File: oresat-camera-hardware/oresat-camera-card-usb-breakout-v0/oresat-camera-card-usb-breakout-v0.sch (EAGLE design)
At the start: 4 parts, among them J2 USB_A_SMT_FEMALE, J3 2-1734592-0

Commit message: first draft finished
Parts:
- added TP1: TEST-POINTPOGO_PTH, SparkFun-Connectors:TEST-POINTPOGO_PTH
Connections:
- new net N$2: J3.17, TP1.1
- net GND: no longer J3.17
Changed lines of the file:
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@@
 <part name="C1" library="oresat-rcl" deviceset="C-EU" device="0603-A" value="100nf"/>
 <part name="GND6" library="SparkFun-PowerSymbols" deviceset="GND" device=""/>
+<part name="TP1" library="SparkFun-Connectors" deviceset="TEST-POINT" device="POGO_PTH"/>
 </parts>
 <sheets>
@@
 <instance part="GND6" gate="1" x="86.36" y="-15.24" smashed="yes">
 <attribute name="VALUE" x="86.36" y="-15.494" size="1.778" layer="96" align="top-center"/>
+</instance>
+<instance part="TP1" gate="G$1" x="55.88" y="27.94" smashed="yes">
+<attribute name="NAME" x="53.34" y="30.48" size="1.778" layer="95" font="vector"/>
 </instance>
 </instances>
@@
 </segment>
 <segment>
-<pinref part="J3" gate="G$1" pin="17"/>
-<wire x1="45.72" y1="27.94" x2="48.26" y2="27.94" width="0.1524" layer="91"/>
-<wire x1="48.26" y1="27.94" x2="48.26" y2="30.48" width="0.1524" layer="91"/>
 <pinref part="J3" gate="G$1" pin="PAD"/>
 <wire x1="48.26" y1="30.48" x2="48.26" y2="33.02" width="0.1524" layer="91"/>
@@
 <pinref part="J3" gate="G$1" pin="18"/>
 <wire x1="45.72" y1="30.48" x2="48.26" y2="30.48" width="0.1524" layer="91"/>
-<junction x="48.26" y="30.48"/>
 <pinref part="GND4" gate="1" pin="GND"/>
 <wire x1="48.26" y1="38.1" x2="53.34" y2="38.1" width="0.1524" layer="91"/>
@@
 </segment>
 </net>
+<net name="N$2" class="0">
+<segment>
+<pinref part="J3" gate="G$1" pin="17"/>
+<pinref part="TP1" gate="G$1" pin="1"/>
+<wire x1="45.72" y1="27.94" x2="55.88" y2="27.94" width="0.1524" layer="91"/>
+</segment>
+</net>

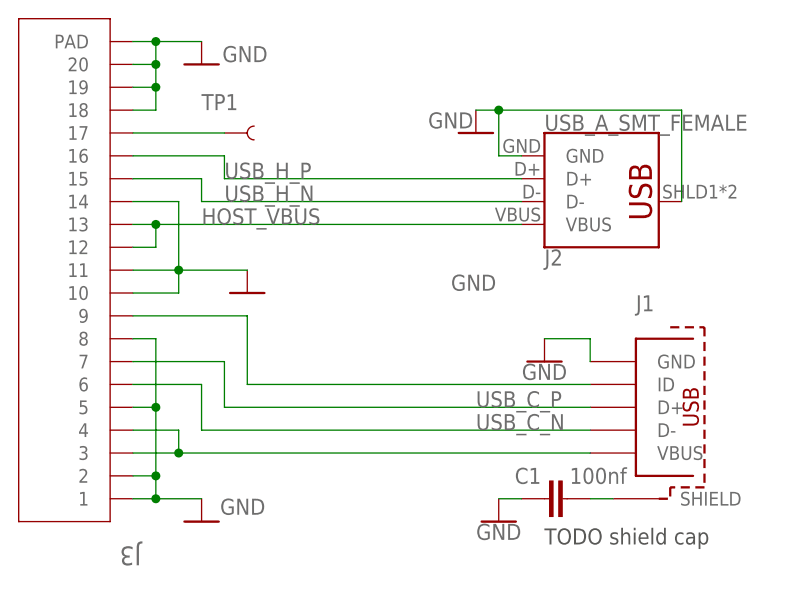
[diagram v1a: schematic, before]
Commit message: added VDD caps
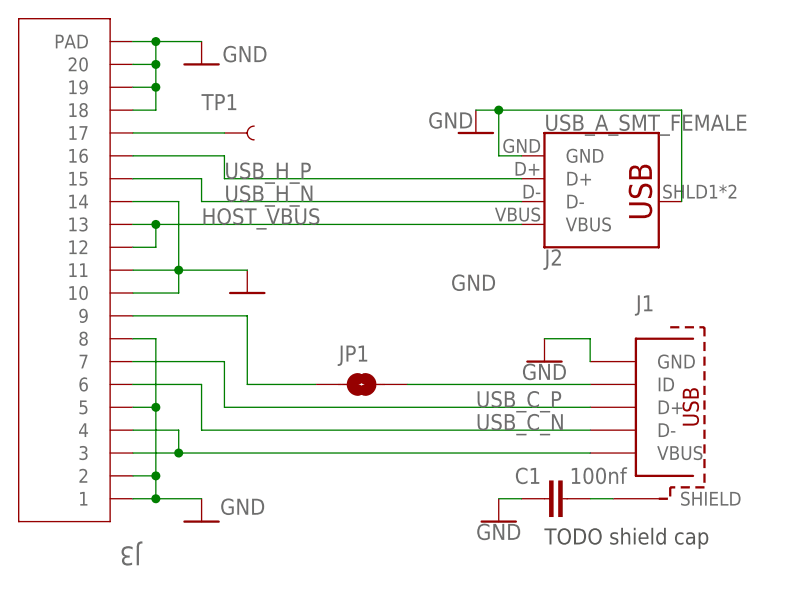
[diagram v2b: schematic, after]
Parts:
- added JP1: JUMPER-SMT_2_NO_SILK, SparkFun-Jumpers:JUMPER-SMT_2_NO_SILK
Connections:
- new net N$3: J1.ID, JP1.2
- net N$5: now also JP1.1; no longer J1.ID
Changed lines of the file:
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@@
 <?xml version="1.0" encoding="utf-8"?>
 <!DOCTYPE eagle SYSTEM "eagle.dtd">
-<eagle version="9.5.0">
+<eagle version="9.4.2">
 <drawing>
 <settings>
@@
 <part name="GND6" library="SparkFun-PowerSymbols" deviceset="GND" device=""/>
 <part name="TP1" library="SparkFun-Connectors" deviceset="TEST-POINT" device="POGO_PTH"/>
+<part name="JP1" library="SparkFun-Jumpers" deviceset="JUMPER-SMT_2_NO" device="_SILK"/>
 </parts>
 <sheets>
@@
 <instance part="TP1" gate="G$1" x="55.88" y="27.94" smashed="yes">
 <attribute name="NAME" x="53.34" y="30.48" size="1.778" layer="95" font="vector"/>
+</instance>
+<instance part="JP1" gate="G$1" x="71.12" y="0" smashed="yes">
+<attribute name="NAME" x="68.58" y="2.54" size="1.778" layer="95" font="vector"/>
 </instance>
 </instances>
@@
 <wire x1="45.72" y1="7.62" x2="58.42" y2="7.62" width="0.1524" layer="91"/>
 <wire x1="58.42" y1="7.62" x2="58.42" y2="0" width="0.1524" layer="91"/>
-<pinref part="J1" gate="G$1" pin="ID"/>
-<wire x1="58.42" y1="0" x2="96.52" y2="0" width="0.1524" layer="91"/>
+<pinref part="JP1" gate="G$1" pin="1"/>
+<wire x1="58.42" y1="0" x2="66.04" y2="0" width="0.1524" layer="91"/>
 </segment>
 </net>
@@
 </segment>
 </net>
+<net name="N$3" class="0">
+<segment>
+<pinref part="JP1" gate="G$1" pin="2"/>
+<pinref part="J1" gate="G$1" pin="ID"/>
+<wire x1="76.2" y1="0" x2="96.52" y2="0" width="0.1524" layer="91"/>
+</segment>
+</net>

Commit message: made a few minor adjustments when I was making the BOMs
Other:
- note removed: "TODO shield cap"
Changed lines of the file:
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@@
 <?xml version="1.0" encoding="utf-8"?>
 <!DOCTYPE eagle SYSTEM "eagle.dtd">
-<eagle version="9.4.2">
+<eagle version="9.5.0">
 <drawing>
 <settings>
@@
 <sheet>
 <plain>
-<text x="91.44" y="-17.78" size="1.778" layer="97">TODO shield cap</text>
 </plain>
 <instances>
